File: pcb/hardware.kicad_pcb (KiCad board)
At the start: 4 copper layers, 174 parts, among them J1 Micro_SD_Card_Det_Hirose_DM3AT, J2 USB_A, J3 USB_A, U1 AS4C512M16D3L-12BIN, U2 A33, U3 TPS62095RGTR, U4 TPS62095RGTR, U5 TPS62095RGTR, U6 TPS62095RGTR, U7 AP131-25, U8 MPM-15-5, Y1 24Mhz, Y2 32.768khz

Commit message: Working on the layout
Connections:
- U1 pad A1: Net-(U1-PadA1) -> +1V35
- U1 pad A8: Net-(U1-PadA8) -> +1V35
- U1 pad A9: Net-(U1-PadA9) -> GND
- U1 pad B1: Net-(U1-PadB1) -> GND
- U1 pad B2: Net-(U1-PadB2) -> +1V35
- U1 pad B3: Net-(U1-PadB3) -> GND
- U1 pad B9: Net-(U1-PadB9) -> GND
- U1 pad C1: Net-(U1-PadC1) -> +1V35
- U1 pad C9: Net-(U1-PadC9) -> +1V35
- U1 pad D1: Net-(U1-PadD1) -> GND
- U1 pad D2: Net-(U1-PadD2) -> +1V35
- U1 pad D8: Net-(U1-PadD8) -> GND
- U1 pad D9: Net-(U1-PadD9) -> +1V35
- U1 pad E1: Net-(U1-PadE1) -> GND
- U1 pad E2: Net-(U1-PadE2) -> GND
- U1 pad E8: Net-(U1-PadE8) -> GND
- U1 pad E9: Net-(U1-PadE9) -> +1V35
- U1 pad F1: Net-(U1-PadF1) -> +1V35
- U1 pad F9: Net-(U1-PadF9) -> GND
- U1 pad G1: Net-(U1-PadG1) -> GND
- U1 pad G7: Net-(U1-PadG7) -> +1V35
- U1 pad G8: Net-(U1-PadG8) -> GND
- U1 pad G9: Net-(U1-PadG9) -> GND
- U1 pad H2: Net-(U1-PadH2) -> +1V35
- U1 pad H9: Net-(U1-PadH9) -> +1V35
- U1 pad J2: Net-(U1-PadJ2) -> GND
- U1 pad J8: Net-(U1-PadJ8) -> GND
- U1 pad K2: Net-(U1-PadK2) -> +1V35
- U1 pad K8: Net-(U1-PadK8) -> +1V35
- U1 pad M1: Net-(U1-PadM1) -> GND
- U1 pad M9: Net-(U1-PadM9) -> GND
- U1 pad N1: Net-(U1-PadN1) -> +1V35
- U1 pad N9: Net-(U1-PadN9) -> +1V35
- U1 pad P1: Net-(U1-PadP1) -> GND
- U1 pad P9: Net-(U1-PadP9) -> GND
- U1 pad R1: Net-(U1-PadR1) -> +1V35
- U1 pad R9: Net-(U1-PadR9) -> +1V35
- U1 pad T1: Net-(U1-PadT1) -> GND
- U1 pad T9: Net-(U1-PadT9) -> GND
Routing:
- net +1V35: track 0.00 -> 3.74 mm, vias 0 -> 6
- net dba1: track 32.1 -> 34.4 mm
- net /ram/!CAS: track 28.1 -> 29.1 mm, vias 1 -> 2
- net GND: track 0.00 -> 0.55 mm, vias 0 -> 3
- added copper zone on In1.Cu, net +1V35
- added copper zone on B.Cu, net GND
- added copper zone on F.Cu, net GND

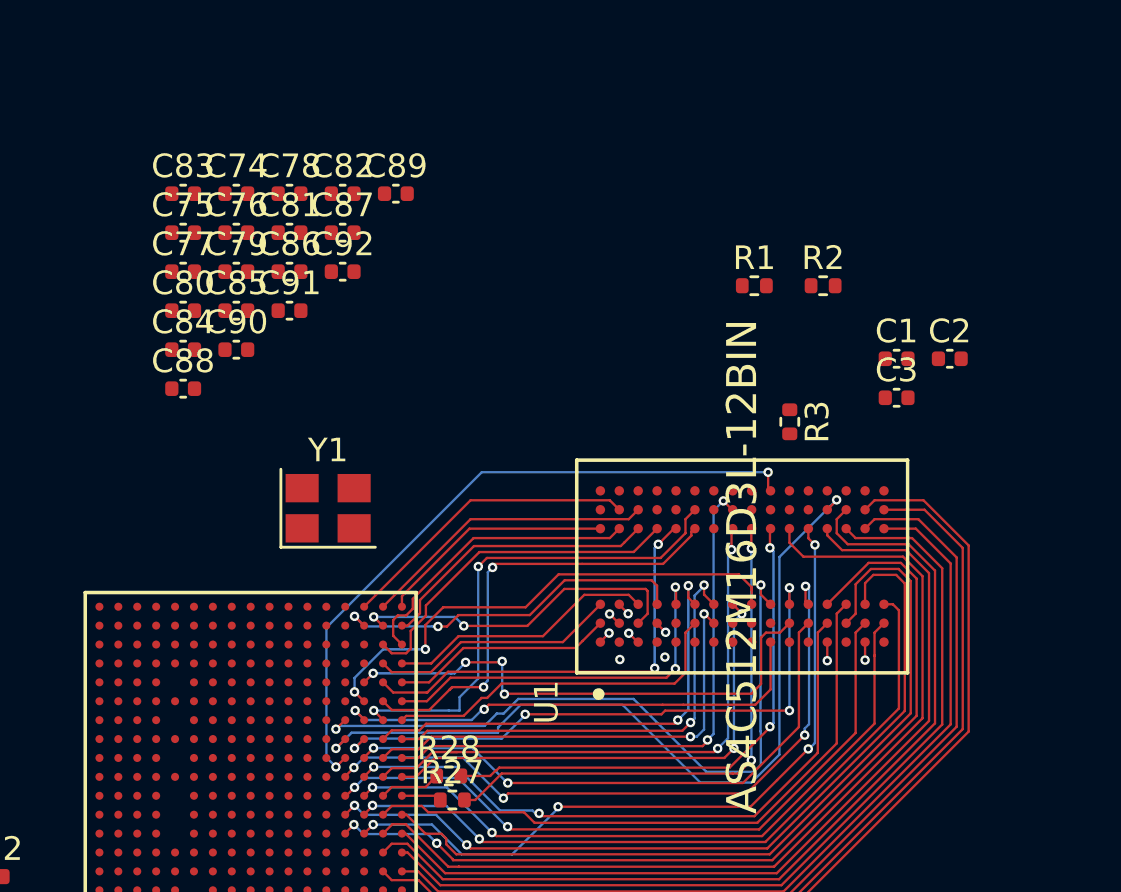
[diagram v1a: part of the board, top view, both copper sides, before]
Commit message: Ram finally hooked up
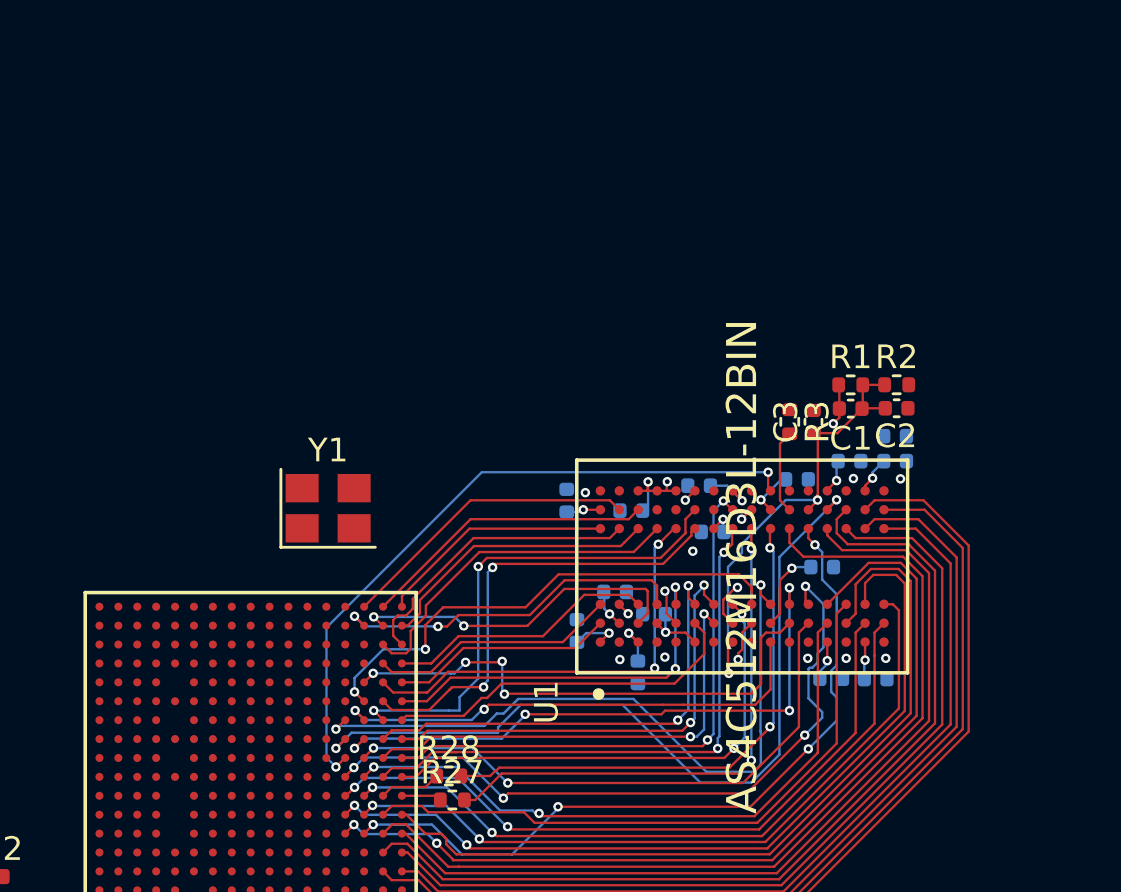
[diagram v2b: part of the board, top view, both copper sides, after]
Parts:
- removed C81, C83, C84, C88: 100nF, Capacitor_SMD:C_0402_1005Metric
- C74, C75, C76, C77, C78, C79, C80, C82, C85, C86, C87, C89, C90, C91, C92: moved to B.Cu
- moved C75 31.6 mm to (142.0, 96.4)
- moved C89 28.9 mm to (141.2, 105.6)
- moved C91 27.7 mm to (139.3, 105.6)
- moved C76 27.7 mm to (140.1, 96.4)
- moved C78 27.6 mm to (142.0, 95.4)
- moved C77 27.4 mm to (137.9, 97.2)
- moved C82 25.7 mm to (138.9, 100.9)
- moved C80 23.1 mm to (133.7, 97.4), turned to 180 degrees
- moved C79 23.0 mm to (134.3, 99.4), turned to 180 degrees
- moved C86 22.5 mm to (131.1, 105.3), turned to 270 degrees
- moved C85 21.8 mm to (131.8, 102.9), turned to 180 degrees
- moved C74 21.4 mm to (130.9, 98.5), turned to 180 degrees
- moved C87 19.6 mm to (128.6, 103.6), turned to 90 degrees
- moved C90 19.0 mm to (130.2, 101.9)
- moved C92 13.6 mm to (128.1, 98.1), turned to 90 degrees
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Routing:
- net +1V35: track 3.74 -> 33.4 mm, vias 6 -> 17
- net Net-(C1-Pad2): track 0.00 -> 19.9 mm, vias 0 -> 2
- net GND: track 0.55 -> 5.04 mm, vias 3 -> 14
- net Net-(R3-Pad2): track 0.00 -> 3.55 mm
- net dba2: track 29.0 -> 30.1 mm
- net adr15: track 30.9 -> 31.9 mm
- added copper zone on In2.Cu, net GND

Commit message: Sync
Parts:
- removed C32, C34, C46, C50: 100nF, Capacitor_SMD:C_0402_1005Metric
- C38, C42, C54: moved to B.Cu
- moved C38 31.9 mm to (116.3, 110.2), turned to 270 degrees
- moved C54 28.3 mm to (115.3, 110.2), turned to 270 degrees
- moved C42 23.5 mm to (115.8, 108.8), turned to 180 degrees
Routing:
- net /ram/!CS: track 22.2 -> 39.1 mm
- net adr15: track 31.9 -> 48.5 mm
- net /ram/!WE: track 25.6 -> 38.9 mm
- net dba0: track 24.7 -> 37.7 mm
- net adr3: track 27.0 -> 37.7 mm
- net /ram/!RST: track 29.0 -> 39.1 mm
- net dba2: track 30.1 -> 37.7 mm
- net adr13: track 30.7 -> 37.4 mm
- net +1V35: track 33.4 -> 39.5 mm, vias 17 -> 18
- net adr2: track 27.1 -> 32.7 mm
- net /ram/ODT: track 20.8 -> 25.4 mm
- net adr7: track 29.3 -> 32.8 mm
- net adr14: track 36.7 -> 39.2 mm
- net adr9: track 35.5 -> 37.8 mm
- net adr0: track 38.1 -> 39.8 mm
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- added copper zone on F.Cu, net +1V35

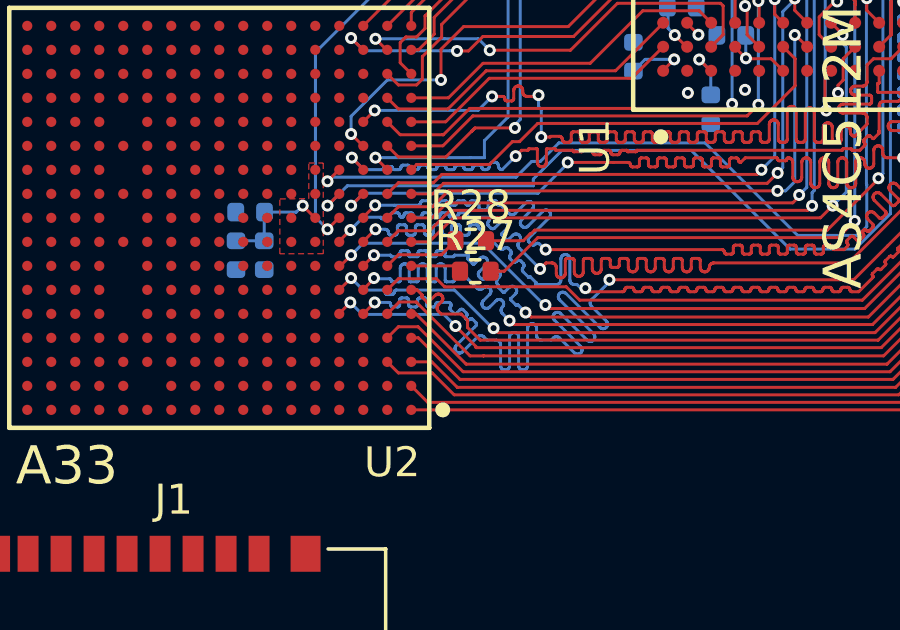
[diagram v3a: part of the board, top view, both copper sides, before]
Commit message: All address buses length matched
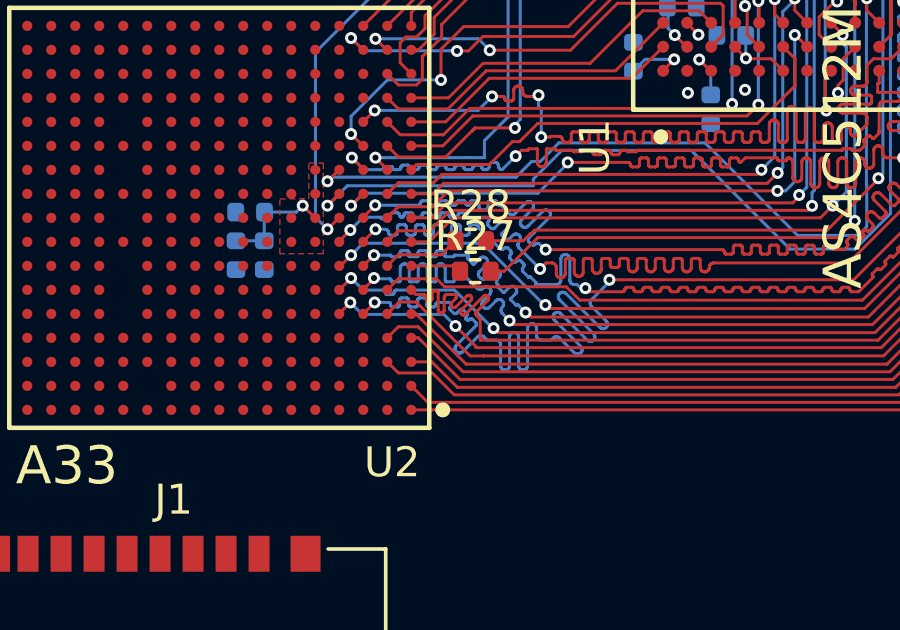
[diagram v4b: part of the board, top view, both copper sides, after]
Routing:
- net adr5: track 35.8 -> 40.1 mm

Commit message: Unsaved changes.
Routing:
- net adr2: track 32.7 -> 38.0 mm
- net adr7: track 32.8 -> 37.3 mm
- net /ram/!RST: track 39.1 -> 37.4 mm
- net adr9: track 37.8 -> 39.1 mm
- net adr12: track 37.2 -> 38.1 mm
- net adr13: track 37.4 -> 38.0 mm

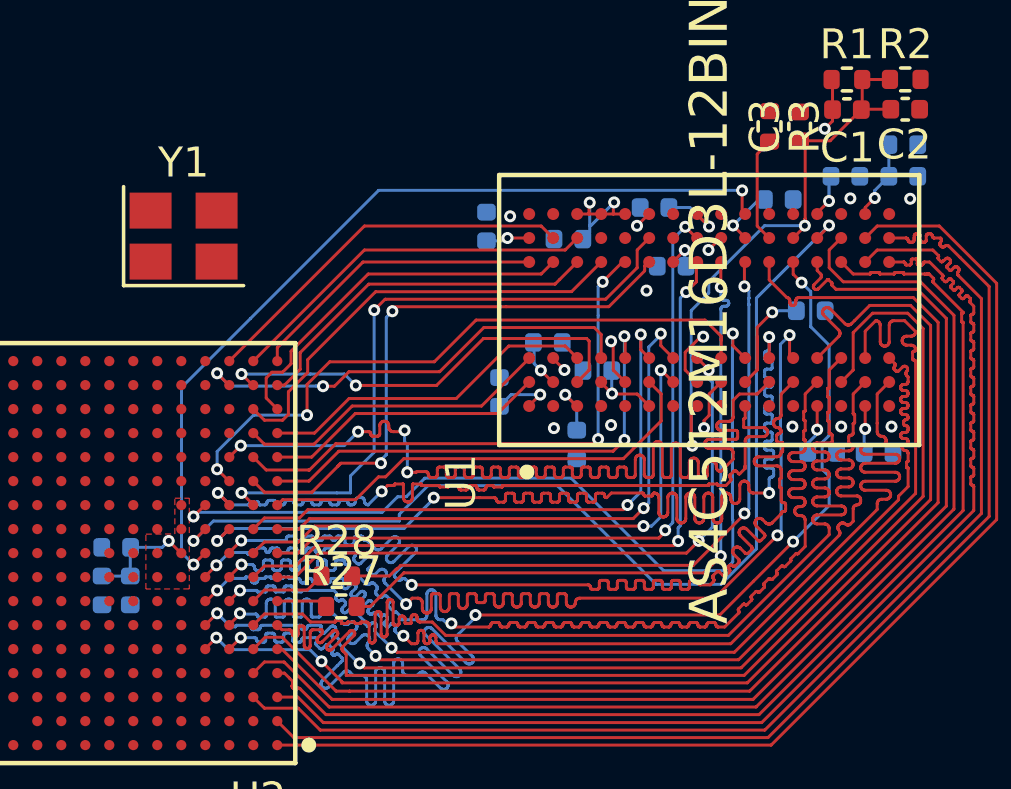
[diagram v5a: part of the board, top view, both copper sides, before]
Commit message: Length matching finally "complete"
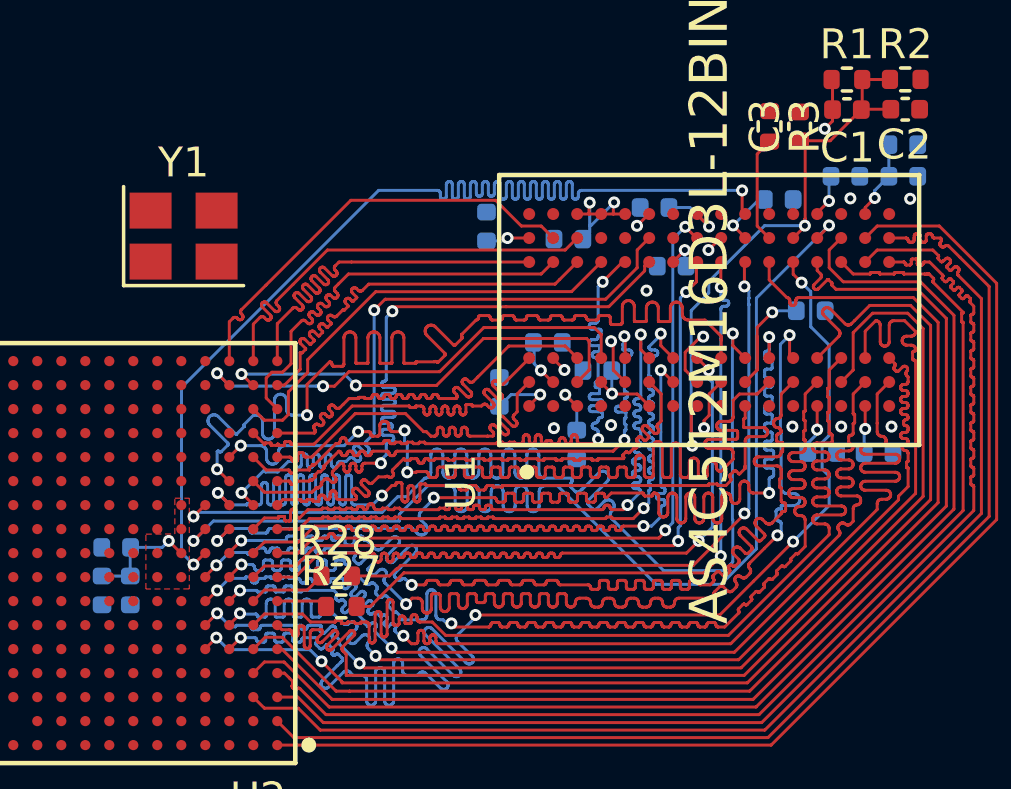
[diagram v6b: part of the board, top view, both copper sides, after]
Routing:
- net /ram/!RAS: track 21.4 -> 38.4 mm
- net /ram/ODT: track 25.4 -> 38.9 mm
- net /ram/!CKE: track 28.9 -> 40.0 mm
- net /ram/!CAS: track 29.1 -> 40.0 mm
- net /ram/LDM: track 18.6 -> 24.2 mm
- net dba1: track 34.4 -> 40.0 mm
- net d6: track 19.5 -> 24.2 mm
- net d13: track 9.43 -> 14.1 mm
- net d1: track 19.6 -> 24.2 mm
- net d9: track 10.0 -> 14.5 mm
- net /ram/LDQS: track 19.7 -> 24.2 mm
- net d2: track 15.4 -> 19.7 mm
- net d15: track 10.5 -> 14.7 mm
- net dba2: track 37.7 -> 41.1 mm
- net d14: track 11.4 -> 14.7 mm
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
